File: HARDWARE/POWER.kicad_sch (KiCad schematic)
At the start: 28 parts, among them J3 1746142-1, SW3 SW_Push, U2 IP5306, U9 AMS1117-3.3

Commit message: Pre position of components
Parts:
- removed D2: LED, LED_SMD:LED_0603_1608Metric, symbol Device:LED
- removed R10: 20R, Resistor_SMD:R_0603_1608Metric, symbol Device:R_Small
- H1, H2, H3, H4: footprint MountingHole:MountingHole_3.2mm_M3_Pad -> MountingHole:MountingHole_2.5mm_Pad
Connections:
- net GND: now also D1.1 (K)
- net VBAT: now also U2.3 (LED2), U2.4 (LED3)
- net at D1.2 (A): now also U2.2 (LED1); no longer U2.4 (LED3)
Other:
- note added: "BATTERY CHARGER"
- note added: "LOW DROPOUT REGULATOR"
- moved on the sheet: C22, C23, C43, C44, C45, C46, D1, D10, R11, R12, R45, SW3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

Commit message: esa
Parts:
- C19, C20, C21: footprint Capacitor_SMD:C_0603_1608Metric -> Capacitor_SMD:C_1206_3216Metric
- L1: footprint Inductor_SMD:L_0603_1608Metric -> Inductor_SMD:L_APV_ANR6020
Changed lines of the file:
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@@
 			)
 		)
-		(property "Footprint" "Capacitor_SMD:C_0603_1608Metric"
+		(property "Footprint" "Capacitor_SMD:C_1206_3216Metric"
 			(at 212.09 60.96 0)
 			(effects
@@
 			)
 		)
-		(property "Footprint" "Capacitor_SMD:C_0603_1608Metric"
+		(property "Footprint" "Capacitor_SMD:C_1206_3216Metric"
 			(at 203.2 60.96 0)
 			(effects
@@
 			)
 		)
-		(property "Footprint" "Capacitor_SMD:C_0603_1608Metric"
+		(property "Footprint" "Capacitor_SMD:C_1206_3216Metric"
 			(at 198.12 60.96 0)
 			(effects
@@
 			)
 		)
-		(property "Footprint" "Inductor_SMD:L_0603_1608Metric"
+		(property "Footprint" "Inductor_SMD:L_APV_ANR6020"
 			(at 156.21 62.23 0)
 			(effects

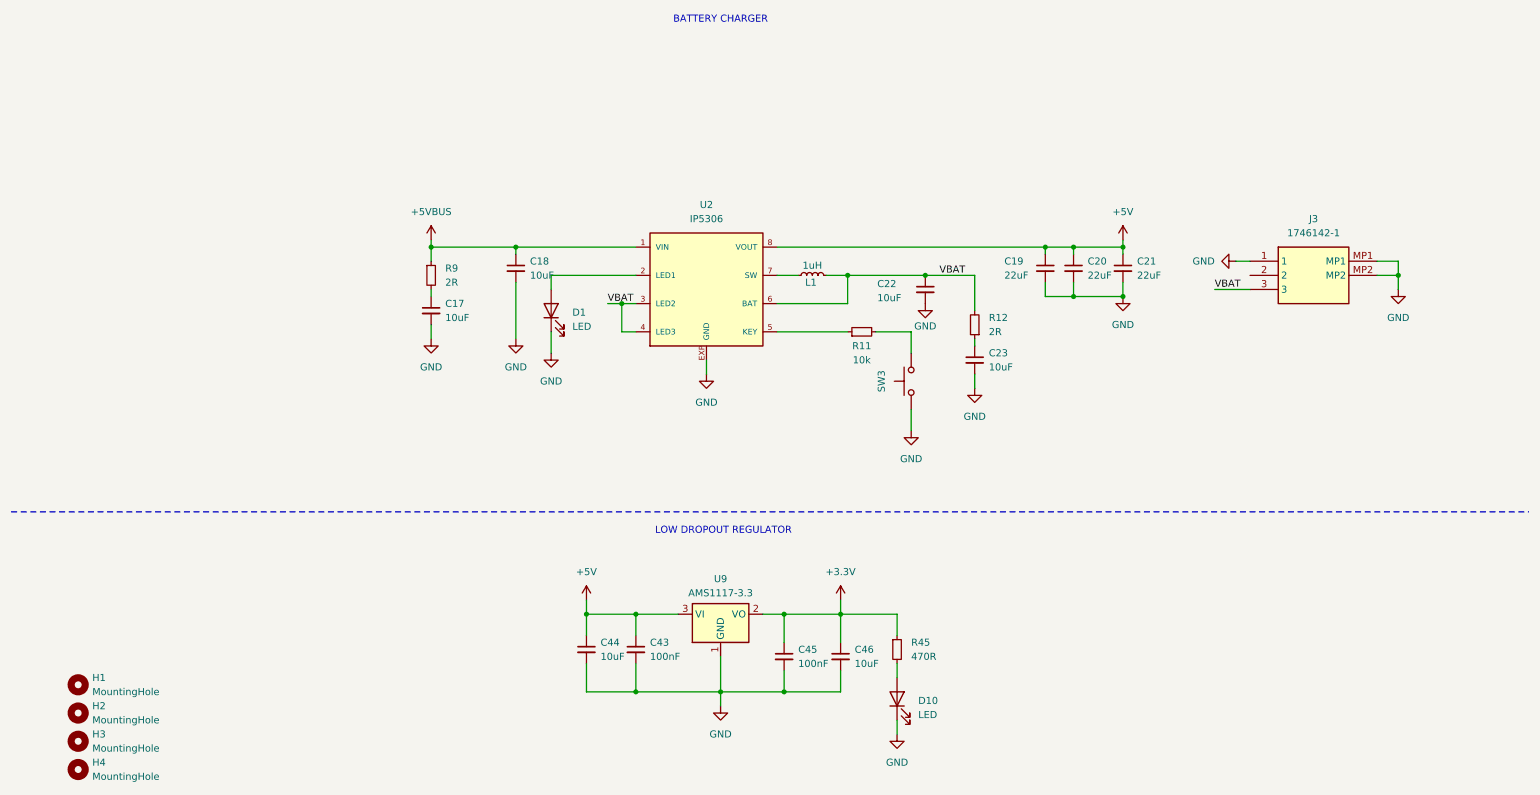
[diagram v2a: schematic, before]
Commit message: fix fpc
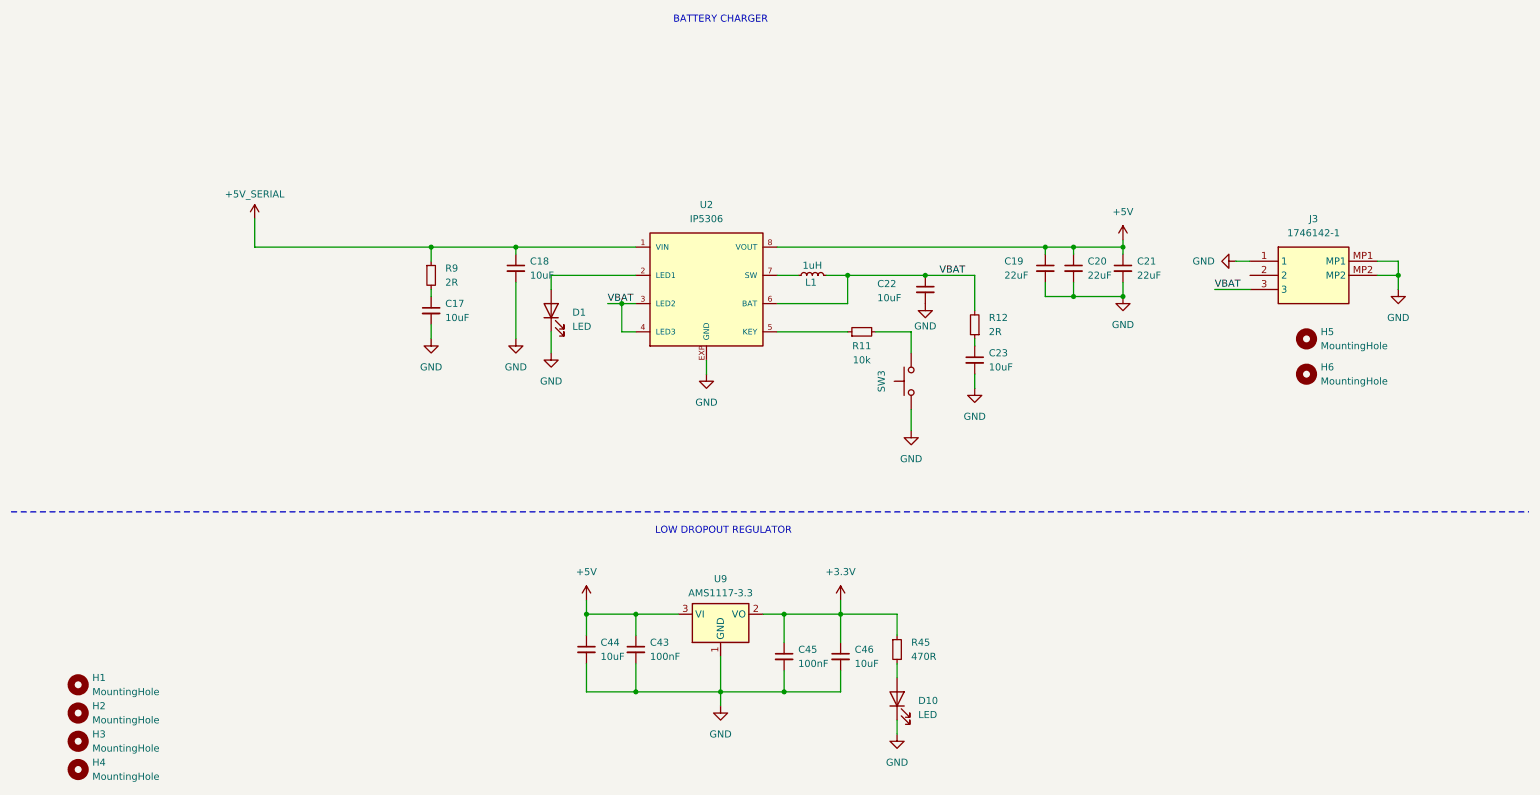
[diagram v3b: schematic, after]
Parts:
- added H5, H6: MountingHole, MountingHole:MountingHole_2.5mm, symbol Mechanical:MountingHole
- C17, C18, C44, C46: footprint Capacitor_SMD:C_0603_1608Metric -> Capacitor_SMD:C_0805_2012Metric
- SW3: footprint Button_Switch_SMD:SW_SPST_CK_RS282G05A3 -> Button_Switch_SMD:SW_Push_1P1T-MP_NO_Horizontal_Alps_SKRTLAE010
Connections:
- net +5VBUS renamed +5V_SERIAL
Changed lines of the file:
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@@
 	)
 	(junction
-		(at 87.63 57.15)
+		(at 261.62 62.23)
 		(diameter 0)
 		(color 0 0 0 0)
 	)
 	(junction
-		(at 261.62 62.23)
+		(at 87.63 57.15)
 		(diameter 0)
 		(color 0 0 0 0)
@@
 	(wire
 		(pts
-			(xy 87.63 55.88) (xy 87.63 57.15)
-		)
-		(stroke
-			(width 0)
-			(type default)
-		)
-	)
-	(wire
-		(pts
 			(xy 261.62 59.69) (xy 261.62 62.23)
 		)
@@
 	(wire
 		(pts
-			(xy 87.63 57.15) (xy 102.87 57.15)
-		)
-		(stroke
-			(width 0)
-			(type default)
-		)
-	)
-	(wire
-		(pts
 			(xy 121.92 72.39) (xy 121.92 67.31)
 		)
@@
 	(wire
 		(pts
+			(xy 87.63 57.15) (xy 87.63 59.69)
+		)
+		(stroke
+			(width 0)
+			(type default)
+		)
+	)
+	(wire
+		(pts
 			(xy 124.46 72.39) (xy 121.92 72.39)
 		)
@@
 	(wire
 		(pts
+			(xy 87.63 57.15) (xy 102.87 57.15)
+		)
+		(stroke
+			(width 0)
+			(type default)
+		)
+	)
+	(wire
+		(pts
 			(xy 261.62 62.23) (xy 261.62 64.77)
 		)
@@
 	(wire
 		(pts
+			(xy 55.88 52.07) (xy 55.88 57.15)
+		)
+		(stroke
+			(width 0)
+			(type default)
+		)
+	)
+	(wire
+		(pts
 			(xy 171.45 123.19) (xy 171.45 127)
 		)
@@
 	(wire
 		(pts
-			(xy 115.57 137.16) (xy 124.46 137.16)
+			(xy 55.88 57.15) (xy 87.63 57.15)
 		)
 		(stroke
@@
 	(wire
 		(pts
-			(xy 198.12 57.15) (xy 198.12 58.42)
+			(xy 115.57 137.16) (xy 124.46 137.16)
 		)
 		(stroke
@@
 	(wire
 		(pts
-			(xy 87.63 57.15) (xy 87.63 59.69)
+			(xy 198.12 57.15) (xy 198.12 58.42)
 		)
 		(stroke
@@
 	)
 	(symbol
+		(lib_id "power:+5V")
+		(at 55.88 52.07 0)
+		(unit 1)
+		(exclude_from_sim no)
+		(in_bom yes)
+		(on_board yes)
+		(dnp no)
+		(fields_autoplaced yes)
+		(property "Reference" "#PWR030"
+			(at 55.88 55.88 0)
+			(effects
+				(font
+					(size 1.27 1.27)
+				)
+				(hide yes)
+			)
+		)
+		(property "Value" "+5V_SERIAL"
+			(at 55.88 47.625 0)
+			(effects
+				(font
+					(size 1.27 1.27)
+				)
+			)
+		)
+		(property "Footprint" ""
+			(at 55.88 52.07 0)
+			(effects
+				(font
+					(size 1.27 1.27)
+				)
+				(hide yes)
+			)
+		)
+		(property "Datasheet" ""
+			(at 55.88 52.07 0)
+			(effects
+				(font
+					(size 1.27 1.27)
+				)
+				(hide yes)
+			)
+		)
+		(property "Description" ""
+			(at 55.88 52.07 0)
+			(effects
+				(font
+					(size 1.27 1.27)
+				)
+				(hide yes)
+			)
+		)
+		(pin "1"
+		)
+		(instances
+			(project "iW-CORE-BOARD"
+				(path "/8e673f85-6c19-4236-92ba-1263b1e08ba7/ced8c1e0-9357-4387-8a18-0f61c1461310"
+					(reference "#PWR030")
+					(unit 1)
+				)
+			)
+		)
+	)
+	(symbol
 		(lib_name "LED_1")
 		(lib_id "Device:LED")
@@
 			)
 		)
-		(property "Footprint" "Capacitor_SMD:C_0603_1608Metric"
+		(property "Footprint" "Capacitor_SMD:C_0805_2012Metric"
 			(at 161.29 130.81 0)
 			(effects
@@
 	)
 	(symbol
+		(lib_name "MountingHole_1")
+		(lib_id "Mechanical:MountingHole")
+		(at 245.11 80.01 0)
+		(unit 1)
+		(exclude_from_sim yes)
+		(in_bom no)
+		(on_board yes)
+		(dnp no)
+		(fields_autoplaced yes)
+		(property "Reference" "H6"
+			(at 247.65 78.7399 0)
+			(effects
+				(font
+					(size 1.27 1.27)
+				)
+				(justify left)
+			)
+		)
+		(property "Value" "MountingHole"
+			(at 247.65 81.2799 0)
+			(effects
+				(font
+					(size 1.27 1.27)
+				)
+				(justify left)
+			)
+		)
+		(property "Footprint" "MountingHole:MountingHole_2.5mm"
+			(at 245.11 80.01 0)
+			(effects
+				(font
+					(size 1.27 1.27)
+				)
+				(hide yes)
+			)
+		)
+		(property "Datasheet" "~"
+			(at 245.11 80.01 0)
+			(effects
+				(font
+					(size 1.27 1.27)
+				)
+				(hide yes)
+			)
+		)
+		(property "Description" "Mounting Hole without connection"
+			(at 245.11 80.01 0)
+			(effects
+				(font
+					(size 1.27 1.27)
+				)
+				(hide yes)
+			)
+		)
+		(instances
+			(project "iW-CORE-BOARD"
+				(path "/8e673f85-6c19-4236-92ba-1263b1e08ba7/ced8c1e0-9357-4387-8a18-0f61c1461310"
+					(reference "H6")
+					(unit 1)
+				)
+			)
+		)
+	)
+	(symbol
 		(lib_id "IP5306:IP5306")
 		(at 137.16 64.77 0)
@@
 	)
 	(symbol
+		(lib_name "MountingHole_1")
+		(lib_id "Mechanical:MountingHole")
+		(at 245.11 73.66 0)
+		(unit 1)
+		(exclude_from_sim yes)
+		(in_bom no)
+		(on_board yes)
+		(dnp no)
+		(fields_autoplaced yes)
+		(property "Reference" "H5"
+			(at 247.65 72.3899 0)
+			(effects
+				(font
+					(size 1.27 1.27)
+				)
+				(justify left)
+			)
+		)
+		(property "Value" "MountingHole"
+			(at 247.65 74.9299 0)
+			(effects
+				(font
+					(size 1.27 1.27)
+				)
+				(justify left)
+			)
+		)
+		(property "Footprint" "MountingHole:MountingHole_2.5mm"
+			(at 245.11 73.66 0)
+			(effects
+				(font
+					(size 1.27 1.27)
+				)
+				(hide yes)
+			)
+		)
+		(property "Datasheet" "~"
+			(at 245.11 73.66 0)
+			(effects
+				(font
+					(size 1.27 1.27)
+				)
+				(hide yes)
+			)
+		)
+		(property "Description" "Mounting Hole without connection"
+			(at 245.11 73.66 0)
+			(effects
+				(font
+					(size 1.27 1.27)
+				)
+				(hide yes)
+			)
+		)
+		(instances
+			(project ""
+				(path "/8e673f85-6c19-4236-92ba-1263b1e08ba7/ced8c1e0-9357-4387-8a18-0f61c1461310"
+					(reference "H5")
+					(unit 1)
+				)
+			)
+		)
+	)
+	(symbol
 		(lib_id "Device:C_Small")
 		(at 124.46 129.54 0)
@@
 			)
 		)
-		(property "Footprint" "Capacitor_SMD:C_0603_1608Metric"
+		(property "Footprint" "Capacitor_SMD:C_0805_2012Metric"
 			(at 102.87 60.96 0)
 			(effects
@@
 			)
 		)
-		(property "Footprint" "Capacitor_SMD:C_0603_1608Metric"
+		(property "Footprint" "Capacitor_SMD:C_0805_2012Metric"
 			(at 87.63 68.58 0)
 			(effects
@@
 	)
 	(symbol
-		(lib_id "power:+5V")
-		(at 87.63 55.88 0)
-		(unit 1)
-		(exclude_from_sim no)
-		(in_bom yes)
-		(on_board yes)
-		(dnp no)
-		(fields_autoplaced yes)
-		(property "Reference" "#PWR062"
-			(at 87.63 59.69 0)
-			(effects
-				(font
-					(size 1.27 1.27)
-				)
-				(hide yes)
-			)
-		)
-		(property "Value" "+5VBUS"
-			(at 87.63 50.8 0)
-			(effects
-				(font
-					(size 1.27 1.27)
-				)
-			)
-		)
-		(property "Footprint" ""
-			(at 87.63 55.88 0)
-			(effects
-				(font
-					(size 1.27 1.27)
-				)
-				(hide yes)
-			)
-		)
-		(property "Datasheet" ""
-			(at 87.63 55.88 0)
-			(effects
-				(font
-					(size 1.27 1.27)
-				)
-				(hide yes)
-			)
-		)
-		(property "Description" ""
-			(at 87.63 55.88 0)
-			(effects
-				(font
-					(size 1.27 1.27)
-				)
-			)
-		)
-		(pin "1"
-		)
-		(instances
-			(project "iW-CORE-BOARD"
-				(path "/8e673f85-6c19-4236-92ba-1263b1e08ba7/ced8c1e0-9357-4387-8a18-0f61c1461310"
-					(reference "#PWR062")
-					(unit 1)
-				)
-			)
-		)
-	)
-	(symbol
 		(lib_id "Device:C_Small")
 		(at 198.12 60.96 0)
@@
 			)
 		)
-		(property "Footprint" "Capacitor_SMD:C_0603_1608Metric"
+		(property "Footprint" "Capacitor_SMD:C_0805_2012Metric"
 			(at 115.57 129.54 0)
 			(effects
@@
 			)
 		)
-		(property "Footprint" "Button_Switch_SMD:SW_SPST_CK_RS282G05A3"
+		(property "Footprint" "Button_Switch_SMD:SW_Push_1P1T-MP_NO_Horizontal_Alps_SKRTLAE010"
 			(at 168.91 81.28 0)
 			(effects
